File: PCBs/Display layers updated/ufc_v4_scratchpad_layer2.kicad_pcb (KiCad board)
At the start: 2 copper layers, 58 x 16.8 mm, 0 parts

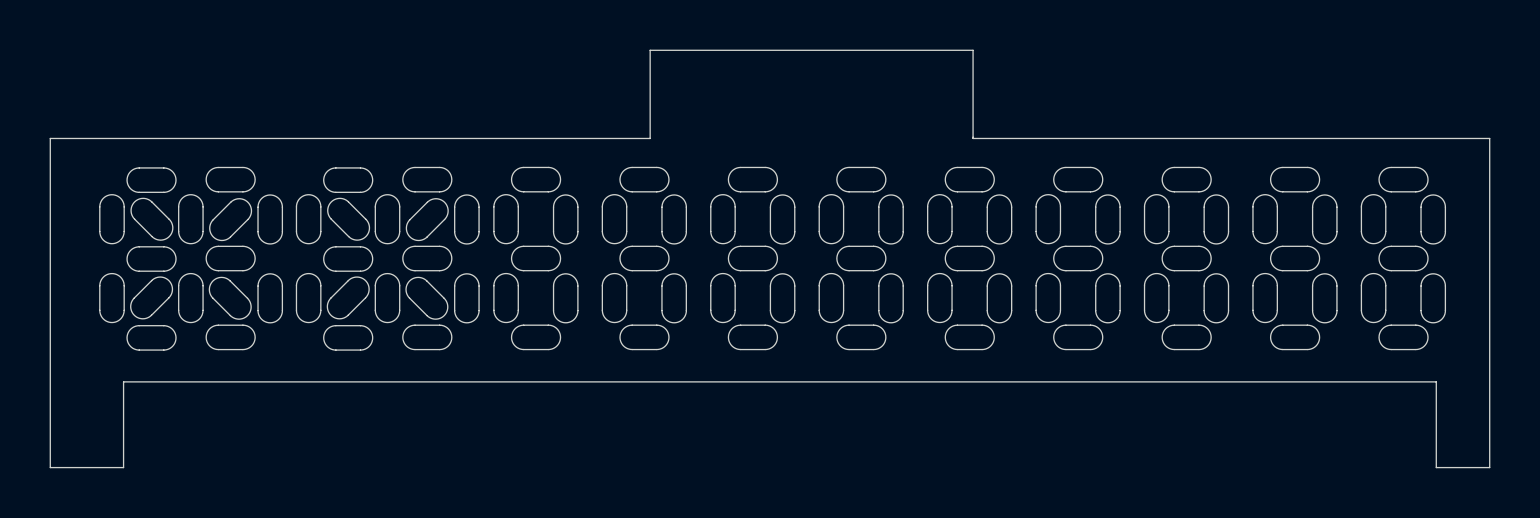
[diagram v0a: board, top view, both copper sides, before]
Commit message: Updated PCBs, cleaned up files
No commit for a while; a lot has happened in the mean time. JLC refused my order for the display layers, so I settled for just the dot layer. The gerbers for the rest are deleted, but the kicad files are still present.

I also received the main PCBs from JLC, and edited a couple small details.
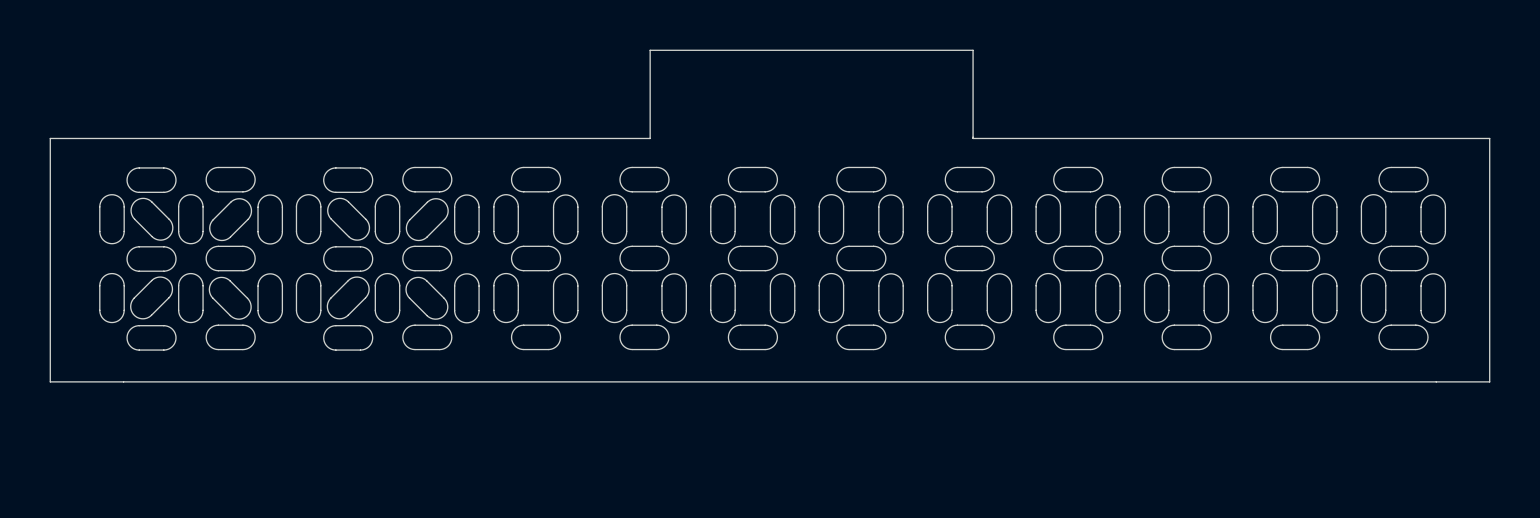
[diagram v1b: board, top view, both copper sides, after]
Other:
- board size 58 x 16.8 mm -> 58 x 13.3 mm
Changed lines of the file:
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@@
   (general
     (thickness 1.6)
-    (drawings 396)
+    (drawings 394)
     (tracks 0)
     (zones 0)
@@
       (usegerberattributes false)
       (usegerberadvancedattributes false)
-      (creategerberjobfile false)
+      (creategerberjobfile true)
       (excludeedgelayer true)
       (linewidth 0.100000)
@@
       (drillshape 0)
       (scaleselection 1)
-      (outputdirectory "gerber"))
+      (outputdirectory "../Gerbers/Display layers/Scratchpad layer 2/"))
   )
   (net 0 "")
@@
     (uvia_drill 0.1)
   )
-  (gr_line (start 106.2375 88.842) (end 109.1875 88.842) (layer Edge.Cuts) (width 0.05))
-  (gr_line (start 106.2375 75.592) (end 106.2375 88.842) (layer Edge.Cuts) (width 0.05))
+  (gr_line (start 106.2375 85.392) (end 109.1875 85.392) (layer Edge.Cuts) (width 0.05))
+  (gr_line (start 106.2375 75.592) (end 106.2375 85.392) (layer Edge.Cuts) (width 0.05))
   (gr_line (start 130.3875 72.042) (end 143.3875 72.042) (layer Edge.Cuts) (width 0.05))
-  (gr_line (start 164.1875 88.842) (end 162.0375 88.842) (layer Edge.Cuts) (width 0.05))
-  (gr_line (start 164.1875 75.592) (end 164.1875 88.842) (layer Edge.Cuts) (width 0.05))
-  (gr_line (start 162.0375 85.392) (end 162.0375 88.842) (layer Edge.Cuts) (width 0.05))
+  (gr_line (start 164.1875 85.392) (end 162.0375 85.392) (layer Edge.Cuts) (width 0.05))
+  (gr_line (start 164.1875 75.592) (end 164.1875 85.392) (layer Edge.Cuts) (width 0.05))
   (gr_line (start 109.1875 85.392) (end 162.0375 85.392) (layer Edge.Cuts) (width 0.05))
-  (gr_line (start 109.1875 88.842) (end 109.1875 85.392) (layer Edge.Cuts) (width 0.05))
   (gr_line (start 143.3875 75.592) (end 164.1875 75.592) (layer Edge.Cuts) (width 0.05))
   (gr_line (start 143.3875 75.542) (end 143.3875 75.592) (layer Edge.Cuts) (width 0.05))
